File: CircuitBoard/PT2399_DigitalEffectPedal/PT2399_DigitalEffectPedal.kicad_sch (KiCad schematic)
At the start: 129 parts, among them J1 POWER_SOURCE, J10 AudioInput_board, J11 AudioJack3_Input, J12 AudioOutput_connector, J13 3PDT_AudioInput, J14 AudioJack3_Output, J15 Encoder_connector, J16 Programming header, J17 Encoder_board_connector, J18 PUSH_STOMP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

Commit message: PCB layout
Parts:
- removed J10, J7: AudioInput_board, Connector_PinHeader_2.54mm:PinHeader_1x06_P2.54mm_Vertical, symbol Connector:Conn_01x06_Pin
- removed J13: 3PDT_AudioInput, Connector_Pin:Pin_D1.0mm_L10.0mm, symbol Connector:Conn_01x01_Pin
- removed J9: 3PDT_AudioIOutput, Connector_Pin:Pin_D1.0mm_L10.0mm, symbol Connector:Conn_01x01_Pin
- added H1, H2, H3, H4: MountingHole, MountingHole:MountingHole_3.2mm_M3, symbol Mechanical:MountingHole
- added J10: 3PDT_AudioIOutput, Connector_Pin:Pin_D1.0mm_L10.0mm, symbol Connector:Conn_01x01_Pin
- added J7: 3PDT_AudioInput, Connector_Pin:Pin_D1.0mm_L10.0mm, symbol Connector:Conn_01x01_Pin
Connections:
- net +5V: now also J16.5 (Pin_5); no longer J16.1 (Pin_1)
- net GNDA: now also J16.4 (Pin_4), J10.1 (Pin_1), J7.1 (Pin_1); no longer J16.2 (Pin_2)
- net LED2_G: now also J16.2 (Pin_2); no longer J16.3 (Pin_3)
- net SIG_OUT: now reaches C22.2, J2.1 (Pin_1)
- net MCLR: now reaches U8.1 (MCLR/VPP)
- net MCLR: now also J16.1 (Pin_1); no longer J16.5 (Pin_5)
- net at U8.28 (RB7/PGD): now also J16.3 (Pin_3); no longer J16.4 (Pin_4)
- net SIG_IN: now reaches C2.1, J5.1 (Pin_1)
- no-connect marks 13 -> 7

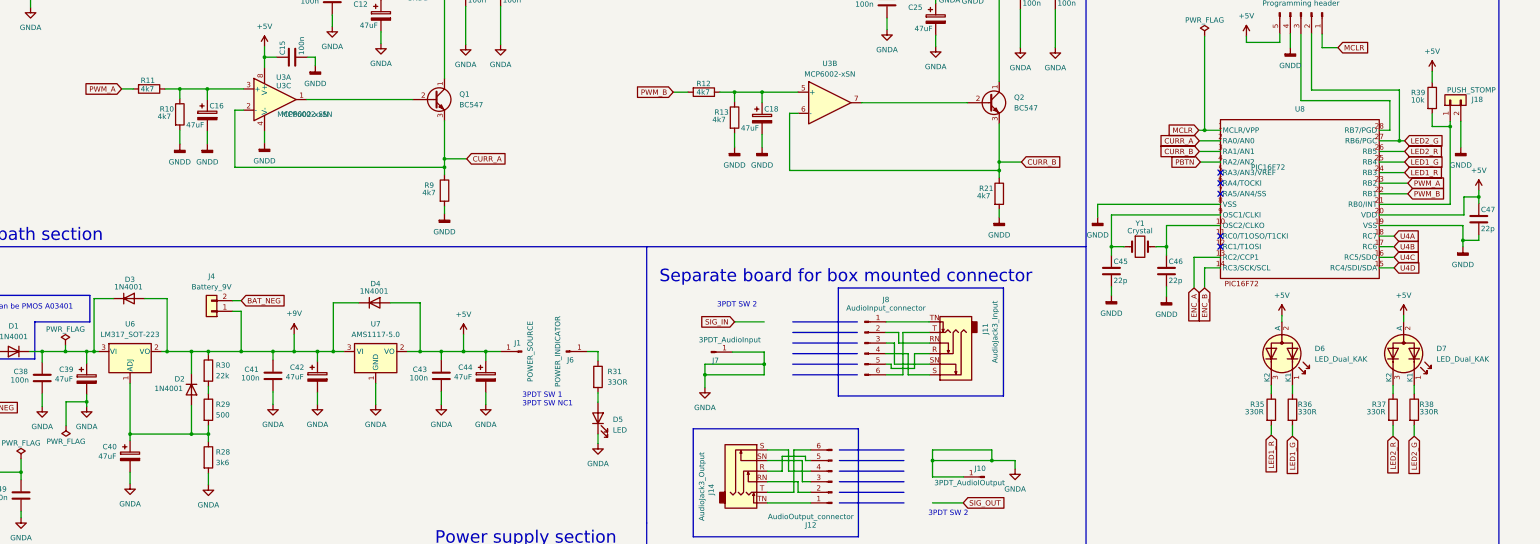
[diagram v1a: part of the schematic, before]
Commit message: PCB layout - main part
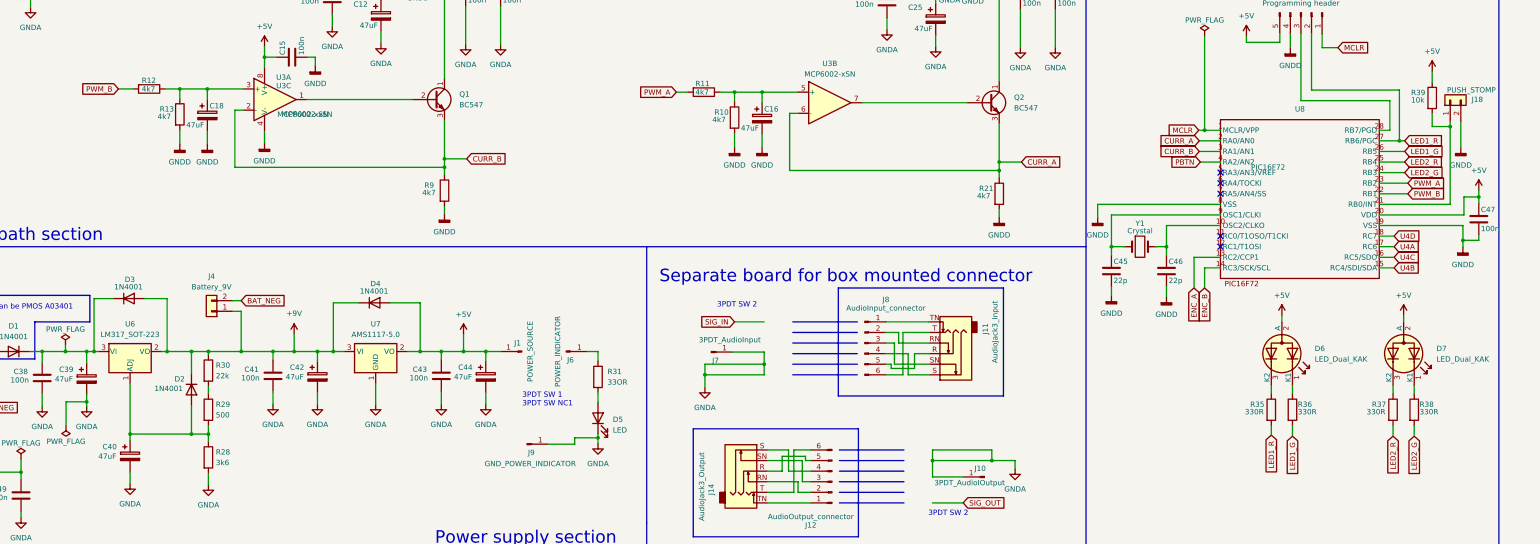
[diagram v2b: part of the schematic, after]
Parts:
- added J9: GND_POWER_INDICATOR, Connector_Pin:Pin_D1.0mm_L10.0mm, symbol Connector:Conn_01x01_Pin
- C47: value 22p -> 100n
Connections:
- net CURR_A: now also Q2.3 (E), R21.1, U3.6 (-); no longer Q1.3 (E), R9.1, U3.2 (-)
- net CURR_B: now also Q1.3 (E), R9.1, U3.2 (-); no longer Q2.3 (E), R21.1, U3.6 (-)
- net GNDA: now also J9.1 (Pin_1)
- net LED1_G: now also U8.26 (RB5); no longer U8.25 (RB4)
- net LED1_R: now also J16.2 (Pin_2), U8.27 (RB6/PGC); no longer U8.24 (RB3)
- net LED2_G: now also U8.24 (RB3); no longer J16.2 (Pin_2), U8.27 (RB6/PGC)
- net LED2_R: now also U8.25 (RB4); no longer U8.26 (RB5)
- net U4A: now also U8.17 (RC6); no longer U8.18 (RC7)
- net U4B: now also U8.15 (RC4/SDI/SDA); no longer U8.17 (RC6)
- net U4D: now also U8.18 (RC7); no longer U8.15 (RC4/SDI/SDA)
- net at C18.1, R12.1, R13.1: now also U3.3 (+); no longer U3.5 (+)
- net at C16.1, R10.1, R11.1: now also U3.5 (+); no longer U3.3 (+)
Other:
- moved on the sheet: C16, C18, R10, R11, R12, R13
